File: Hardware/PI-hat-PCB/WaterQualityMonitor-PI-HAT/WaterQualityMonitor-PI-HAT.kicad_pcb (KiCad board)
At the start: 2 copper layers, 65 x 56 mm, 5 parts, among them J1 GPIO

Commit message: Started new pcb design
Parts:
- added C1: 10uF, SmacSYs:SOIC127P600X175-8N, F.Cu at (212.2, 87.9)
- added C10: 100n, Capacitor_SMD:C_1206_3216Metric_Pad1.33x1.80mm_HandSolder, F.Cu at (248.2, 114.3)
- added C11: 22u 10V, Capacitor_SMD:C_1206_3216Metric_Pad1.33x1.80mm_HandSolder, F.Cu at (245.3, 111.0)
- added C12: 22u 10V, Capacitor_SMD:C_1206_3216Metric_Pad1.33x1.80mm_HandSolder, F.Cu at (242.2, 120.9)
- added C13: 100n, Capacitor_SMD:C_1206_3216Metric_Pad1.33x1.80mm_HandSolder, F.Cu at (242.2, 117.4)
- added C14: 0.1uF, Capacitor_SMD:C_1206_3216Metric_Pad1.33x1.80mm_HandSolder, F.Cu at (310.8, 100.6)
- added C15: 0.1uF, Capacitor_SMD:C_1206_3216Metric_Pad1.33x1.80mm_HandSolder, F.Cu at (293.5, 122.5)
- added C16: 10u, Capacitor_SMD:C_1206_3216Metric_Pad1.33x1.80mm_HandSolder, F.Cu at (218.9, 117.8)
- added C17: 10u, Capacitor_SMD:C_1206_3216Metric_Pad1.33x1.80mm_HandSolder, F.Cu at (203.8, 126.8)
- added C18: 10u, Capacitor_SMD:C_1206_3216Metric_Pad1.33x1.80mm_HandSolder, F.Cu at (203.8, 130.1)
- added C19: 2.7n, Capacitor_SMD:C_1206_3216Metric_Pad1.33x1.80mm_HandSolder, F.Cu at (203.8, 133.5)
- added C2: 0.1uF, Capacitor_SMD:C_1206_3216Metric_Pad1.33x1.80mm_HandSolder, F.Cu at (226.4, 90.3)
- added C20: 100n, Capacitor_SMD:C_1206_3216Metric_Pad1.33x1.80mm_HandSolder, F.Cu at (223.3, 114.3)
- added C21: 22u 10V, Capacitor_SMD:C_1206_3216Metric_Pad1.33x1.80mm_HandSolder, F.Cu at (223.3, 111.0)
- added C22: 22u 10V, Capacitor_SMD:C_1206_3216Metric_Pad1.33x1.80mm_HandSolder, F.Cu at (212.9, 120.3)
- added C23: 100n, Capacitor_SMD:C_1206_3216Metric_Pad1.33x1.80mm_HandSolder, F.Cu at (209.8, 126.8)
- added C24: 100n, Capacitor_SMD:C_1206_3216Metric_Pad1.33x1.80mm_HandSolder, F.Cu at (217.3, 114.4)
- added C25: 100n, Capacitor_SMD:C_1206_3216Metric_Pad1.33x1.80mm_HandSolder, F.Cu at (221.8, 97.5)
- added C3: 47uF, Capacitor_SMD:C_1206_3216Metric_Pad1.33x1.80mm_HandSolder, F.Cu at (258.0, 65.8)
- added C4: 4.7uF, Capacitor_SMD:C_1206_3216Metric_Pad1.33x1.80mm_HandSolder, F.Cu at (249.2, 70.9)
- added C5: 10u, Capacitor_SMD:C_1206_3216Metric_Pad1.33x1.80mm_HandSolder, F.Cu at (269.1, 49.2)
- added C6: 10u, Capacitor_SMD:C_1206_3216Metric_Pad1.33x1.80mm_HandSolder, F.Cu at (236.2, 120.9)
- added C7: 10u, Capacitor_SMD:C_1206_3216Metric_Pad1.33x1.80mm_HandSolder, F.Cu at (251.3, 111.0)
- added C8: 10u, Capacitor_SMD:C_1206_3216Metric_Pad1.33x1.80mm_HandSolder, F.Cu at (236.2, 127.6)
- added C9: 2.7n, Capacitor_SMD:C_1206_3216Metric_Pad1.33x1.80mm_HandSolder, F.Cu at (236.2, 124.2)
- added D1: SESD0402X1UN-0020-090, SmacSYs:SESD0402X1UN0020090, F.Cu at (250.1, 74.7)
- added D2: OVLEW1CB9, SmacSYs:OVLEW1CB9, F.Cu at (212.9, 101.7)
- added D3: SMBJ26A, Snapeda:DIOM4336X265N, F.Cu at (250.9, 66.7)
- added F1: 0.5A, Fuse:Fuse_1206_3216Metric_Pad1.42x1.75mm_HandSolder, F.Cu at (245.2, 74.2)
- added F2: 4A, Fuse:Fuse_1206_3216Metric_Pad1.42x1.75mm_HandSolder, F.Cu at (232.4, 90.2)
- added F3: 3.2A, Fuse:Fuse_1206_3216Metric_Pad1.42x1.75mm_HandSolder, F.Cu at (255.2, 70.9)
- added F4: 10A, Fuse:Fuse_1206_3216Metric_Pad1.42x1.75mm_HandSolder, F.Cu at (226.4, 93.6)
- added FB1: 150uH, Inductor_SMD:L_1206_3216Metric_Pad1.22x1.90mm_HandSolder, F.Cu at (249.2, 59.8)
- added IC1: P82B96TD,118, SmacSYs:SOIC127P600X175-8N, F.Cu at (214.5, 94.5)
- added IC2: DMMT5401-7-F, SmacSYs:SOT95P285X140-6N, F.Cu at (235.8, 134.8)
- added J10: GPIO, Connector_PinSocket_2.54mm:PinSocket_2x20_P2.54mm_Vertical, F.Cu at (205.6, 46.4)
- added J2: Screw_Terminal_01x04, TerminalBlock:TerminalBlock_Altech_AK300-4_P5.00mm, F.Cu at (233.5, 51.1)
- added J3: Screw_Terminal_01x04, TerminalBlock:TerminalBlock_Altech_AK300-4_P5.00mm, F.Cu at (211.3, 51.1)
- added J4: Screw_Terminal_01x02, TerminalBlock:TerminalBlock_Altech_AK300-2_P5.00mm, F.Cu at (237.3, 65.0)
- added J5: Jack-DC 12V+, Connector_BarrelJack:BarrelJack_Wuerth_6941xx301002, F.Cu at (227.2, 60.0)
- added J6: SM04B-SRSS-TB(LF)(SN), Snapeda:JST_SM04B-SRSS-TB(LF)(SN), F.Cu at (238.1, 76.2)
- added JP1: ID_WP, Jumper:SolderJumper-2_P1.3mm_Open_RoundedPad1.0x1.5mm, F.Cu at (219.5, 79.8)
- added L1: 4.7uH, Inductor_SMD:L_1206_3216Metric_Pad1.22x1.90mm_HandSolder, F.Cu at (269.2, 45.8)
- added L2: 15u, Inductor_SMD:L_1206_3216Metric_Pad1.22x1.90mm_HandSolder, F.Cu at (236.2, 117.5)
- added L3: 15u, Inductor_SMD:L_1206_3216Metric_Pad1.22x1.90mm_HandSolder, F.Cu at (217.3, 111.0)
- added M1: Fan, Connector_PinHeader_2.54mm:PinHeader_1x02_P2.54mm_Vertical, F.Cu at (221.1, 90.9)
- added PE1: PeltierElement, TerminalBlock:TerminalBlock_Altech_AK300-2_P5.00mm, F.Cu at (225.0, 81.6)
- added PS1: TSR_2-2433, Converter_DCDC:Converter_DCDC_TRACO_TSR-1_THT, F.Cu at (205.1, 115.7)
- added Q1: IRL540SPBF, SmacSYs:IRL540SPBF, F.Cu at (259.3, 45.6)
- added Q2: IRL540SPBF, SmacSYs:IRL540SPBF, F.Cu at (214.8, 59.6)
- added Q3: DMG2305UX-7, Snapeda:SOT91P240X110-3N_DMG2305UX-7, F.Cu at (247.9, 124.8)
- added R1: 0.2, Resistor_SMD:R_1206_3216Metric_Pad1.30x1.75mm_HandSolder, F.Cu at (269.1, 52.5)
- added R10: 10k, Resistor_SMD:R_1206_3216Metric_Pad1.30x1.75mm_HandSolder, F.Cu at (236.1, 130.9)
- added R11: 10k, Resistor_SMD:R_1206_3216Metric_Pad1.30x1.75mm_HandSolder, F.Cu at (254.2, 114.3)
- added R12: 47K, Resistor_SMD:R_1206_3216Metric_Pad1.30x1.75mm_HandSolder, F.Cu at (257.3, 110.9)
- added R13: 178k, Resistor_SMD:R_1206_3216Metric_Pad1.30x1.75mm_HandSolder, F.Cu at (203.8, 136.8)
- added R14: 10k, Resistor_SMD:R_1206_3216Metric_Pad1.30x1.75mm_HandSolder, F.Cu at (209.8, 130.1)
- added R15: 24k, Resistor_SMD:R_1206_3216Metric_Pad1.30x1.75mm_HandSolder, F.Cu at (215.8, 124.4)
- added R16: 10k, Resistor_SMD:R_1206_3216Metric_Pad1.30x1.75mm_HandSolder, F.Cu at (224.9, 117.6)
- added R17: 1k87, Resistor_SMD:R_1206_3216Metric_Pad1.30x1.75mm_HandSolder, F.Cu at (218.9, 121.1)
- added R18: 3.9k, Resistor_SMD:R_1206_3216Metric_Pad1.30x1.75mm_HandSolder, F.Cu at (245.2, 77.5)
- added R19: 3.9k, Resistor_SMD:R_1206_3216Metric_Pad1.30x1.75mm_HandSolder, F.Cu at (236.9, 83.3)
- added R2: 5.1, Resistor_SMD:R_1206_3216Metric_Pad1.30x1.75mm_HandSolder, F.Cu at (221.1, 100.8)
- added R3: 1.20KOHM-0603-1_10W-1%, Resistor_SMD:R_1206_3216Metric_Pad1.30x1.75mm_HandSolder, F.Cu at (236.9, 86.6)
- added R4: 10K, Resistor_SMD:R_1206_3216Metric_Pad1.30x1.75mm_HandSolder, F.Cu at (275.2, 45.7)
- added R5: 10K, Resistor_SMD:R_1206_3216Metric_Pad1.30x1.75mm_HandSolder, F.Cu at (275.2, 49.0)
- added R6: 178k, Resistor_SMD:R_1206_3216Metric_Pad1.30x1.75mm_HandSolder, F.Cu at (242.1, 124.2)
- added R7: 24k, Resistor_SMD:R_1206_3216Metric_Pad1.30x1.75mm_HandSolder, F.Cu at (248.2, 117.6)
- added R8: 10k, Resistor_SMD:R_1206_3216Metric_Pad1.30x1.75mm_HandSolder, F.Cu at (242.1, 127.5)
- added R9: 1k87, Resistor_SMD:R_1206_3216Metric_Pad1.30x1.75mm_HandSolder, F.Cu at (248.1, 120.9)
- added U1: DRV8870DDA, Package_SO:Texas_HTSOP-8-1EP_3.9x4.9mm_P1.27mm_EP2.95x4.9mm_Mask2.4x3.1mm_ThermalVias, F.Cu at (205.5, 100.2)
- added U2: TPS61169DCKR, Snapeda:SOT65P210X110-5N, F.Cu at (219.3, 86.5)
- added U3: TMC2208_SILENTSTEPSTICK, Footprints:TMC2208_SILENTSTEPSTICK, F.Cu at (298.9, 76.9)
- added U4: TMC2208_SILENTSTEPSTICK, Footprints:TMC2208_SILENTSTEPSTICK, F.Cu at (298.9, 55.0)
- added U5: RT7272AGSP, Snapeda:SOIC127P599X175-9N, F.Cu at (238.0, 112.5)
- added U6: TMC2208_SILENTSTEPSTICK, Footprints:TMC2208_SILENTSTEPSTICK, F.Cu at (298.9, 109.8)
- added U7: DRV8838, Package_SON:WSON-8-1EP_2x2mm_P0.5mm_EP0.9x1.6mm, F.Cu at (292.6, 125.9)
- added U8: RT7272AGSP, Snapeda:SOIC127P599X175-9N, F.Cu at (205.7, 121.9)
- added U9: CAT24C256, Footprints:SOIC127P600X175-8N, F.Cu at (213.1, 81.3)
- J1: value GPIO -> Screw_Terminal_01x04; footprint Connector_PinSocket_2.54mm:PinSocket_2x20_P2.54mm_Vertical -> TerminalBlock:TerminalBlock_Altech_AK300-4_P5.00mm
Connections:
- J1 pad 1: +3V3 -> /FluidMotors/OA1MAIN
- J1 pad 2: +5V -> /FluidMotors/OA2MAIN
- J1 pad 3: /GPIO[2]/SDA1 -> /FluidMotors/OB1MAIN
- J1 pad 4: +5V -> /FluidMotors/OB2MAIN

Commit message: standard pi hat layout finsished
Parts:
- moved J1 254.1 mm to (338.9, 155.5)
- moved C18 90.8 mm to (192.0, 220.2)
- moved J5 90.8 mm to (215.4, 150.1)
- moved L1 90.8 mm to (257.4, 135.9)
- moved Q2 90.8 mm to (203.0, 149.7)
- moved R1 90.8 mm to (257.3, 142.6)
- moved C11 90.8 mm to (233.5, 201.0)
- moved C12 90.8 mm to (230.3, 210.9)
- moved C15 90.8 mm to (281.7, 212.5)
- moved C16 90.8 mm to (207.1, 207.8)
- moved C17 90.8 mm to (192.0, 216.9)
- moved C2 90.8 mm to (214.6, 180.3)
- moved C21 90.8 mm to (211.5, 201.0)
- moved C23 90.8 mm to (198.0, 216.9)
- moved C3 90.8 mm to (246.2, 155.8)
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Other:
- board text removed: "Extend PCB edge 0.5mm if using SMT header"

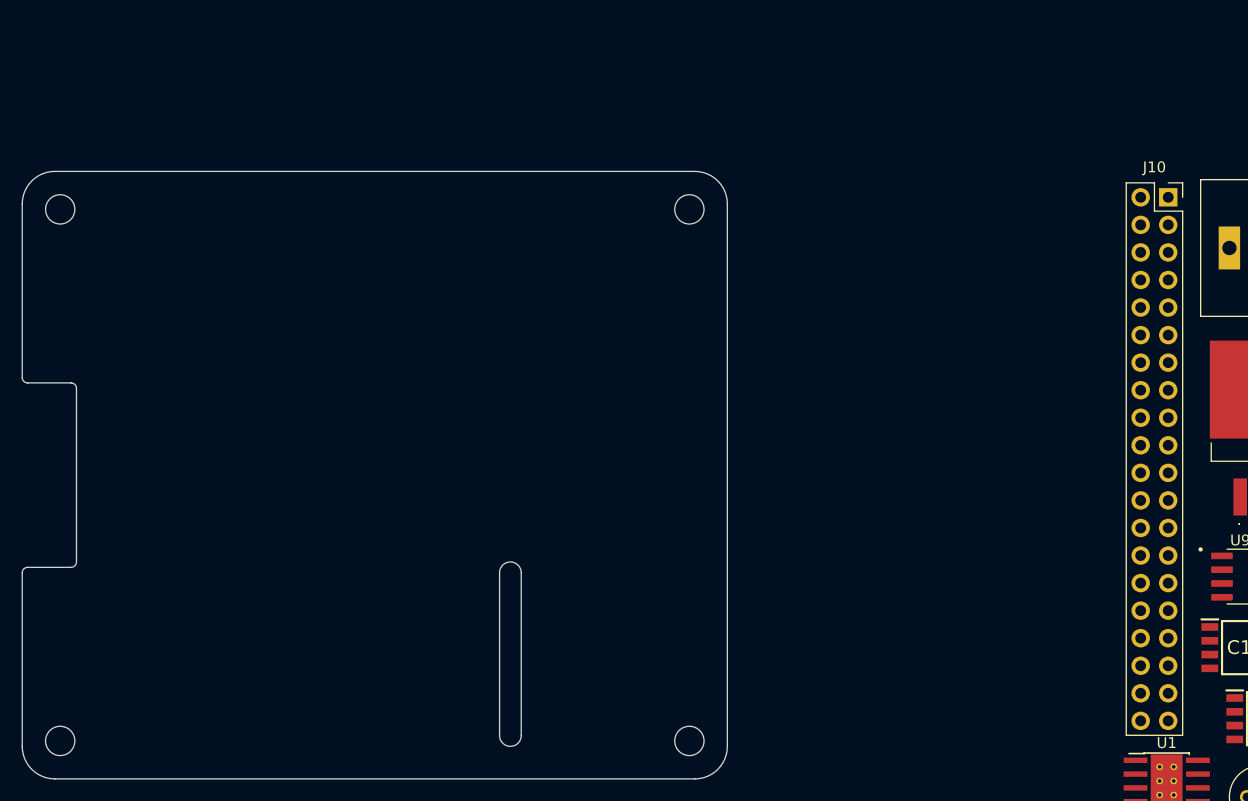
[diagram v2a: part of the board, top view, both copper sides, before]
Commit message: GPIO header moved, hopefully centered
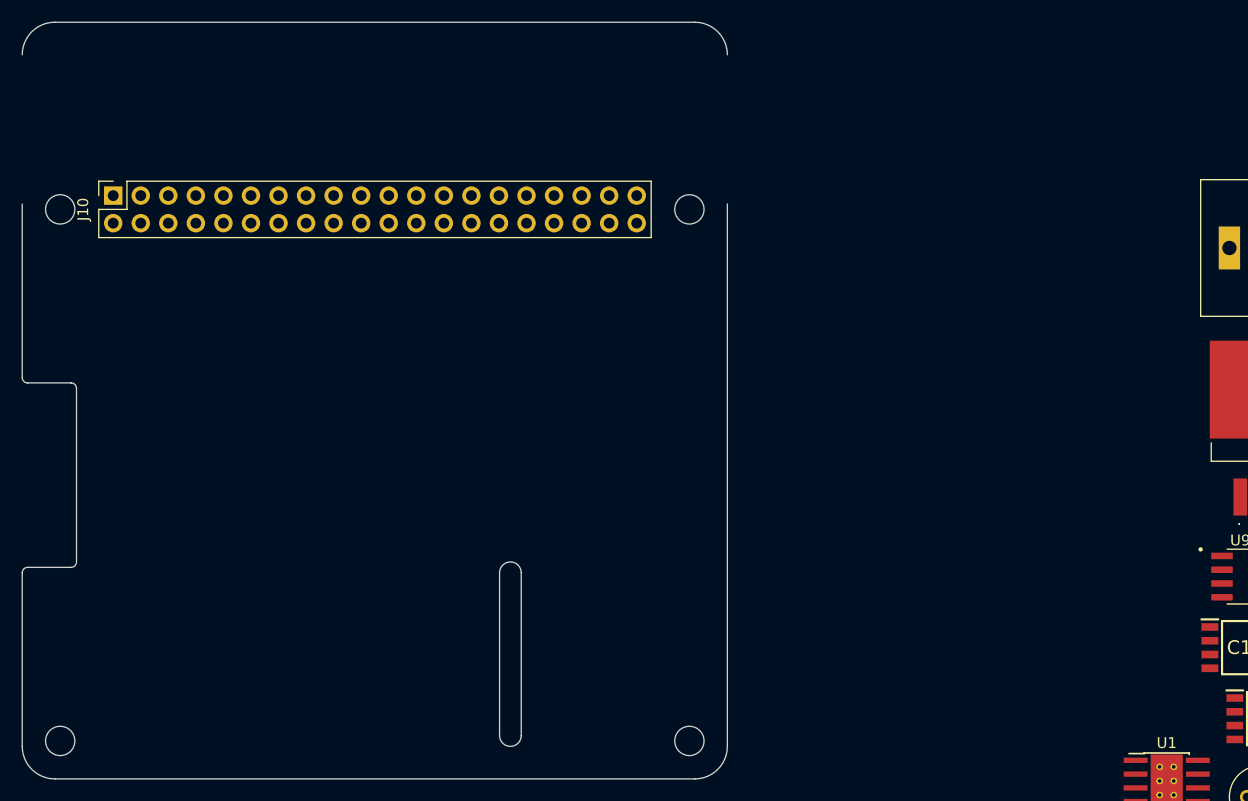
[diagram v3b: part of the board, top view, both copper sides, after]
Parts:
- moved J10 97.3 mm to (96.6, 136.3), turned to 90 degrees
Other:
- board size 65 x 56 mm -> 65 x 69.8 mm

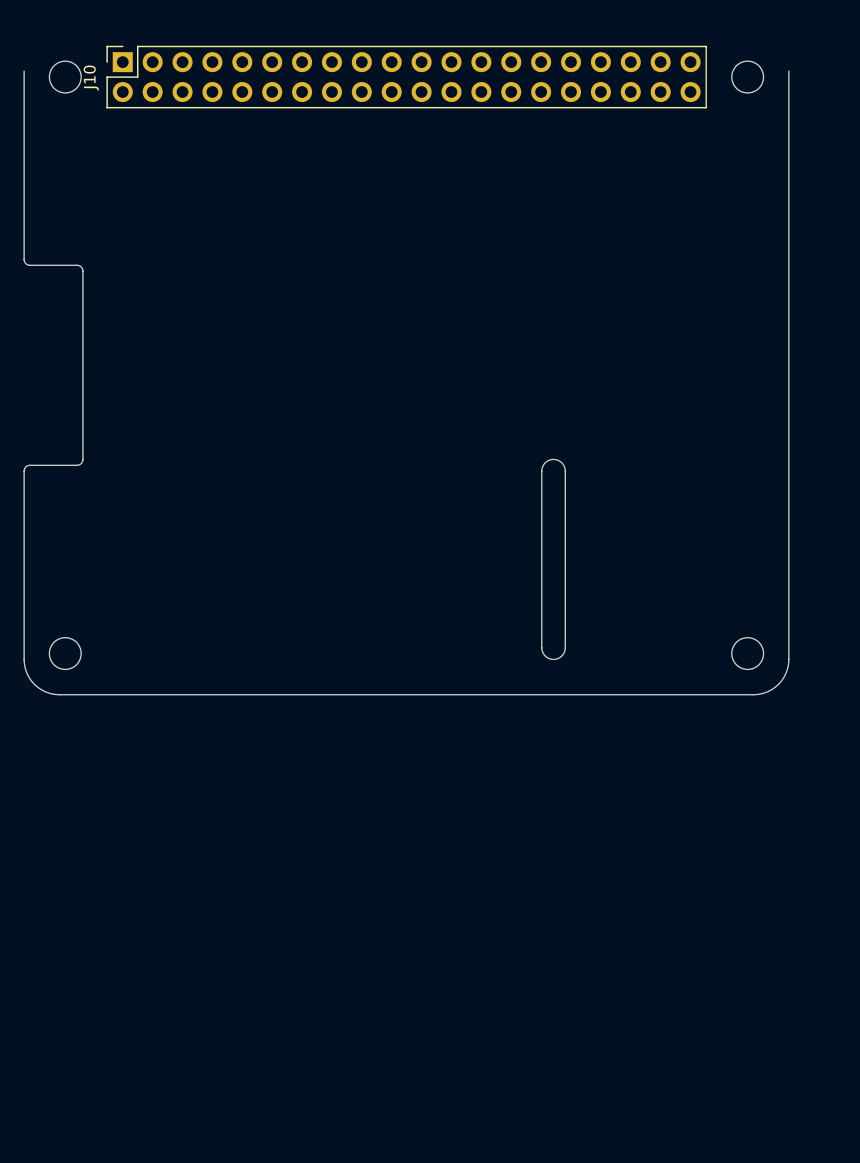
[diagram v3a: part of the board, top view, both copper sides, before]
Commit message: Enlarged hat even further
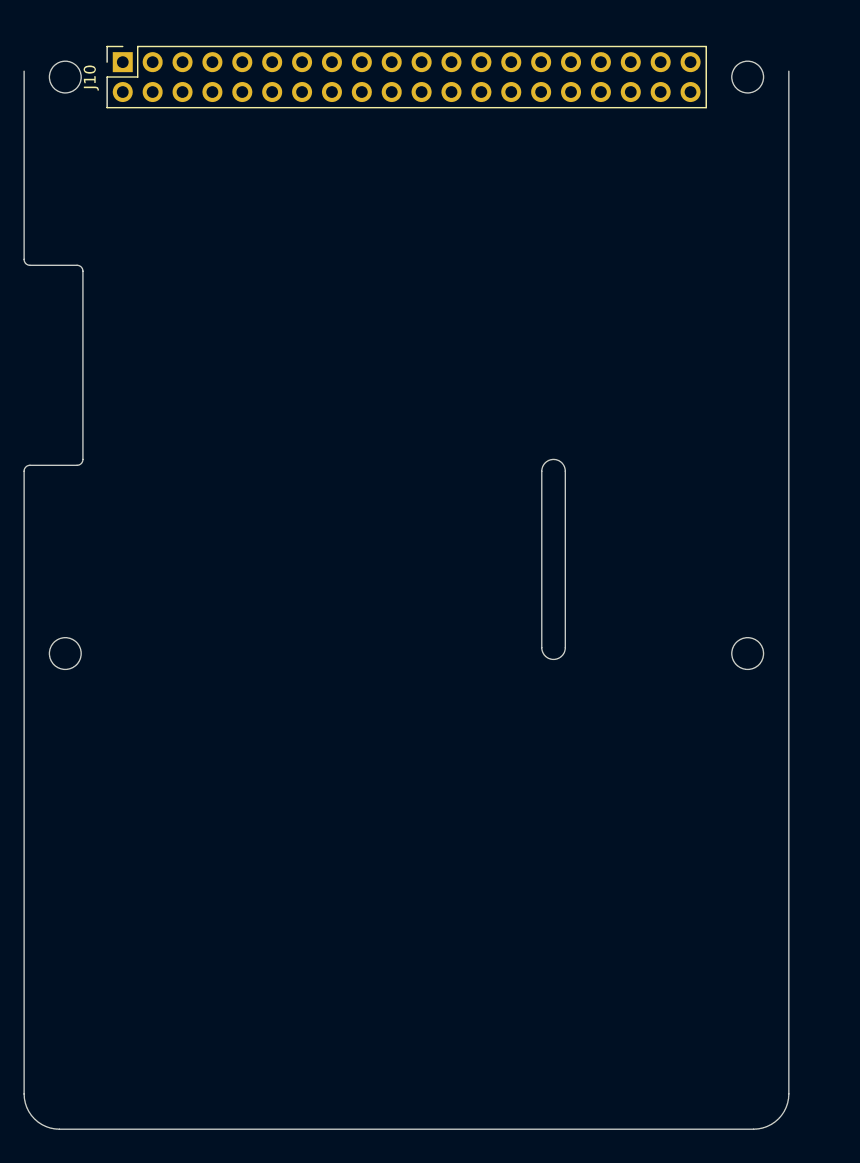
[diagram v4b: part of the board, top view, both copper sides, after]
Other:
- board size 65 x 69.8 mm -> 65 x 106.7 mm
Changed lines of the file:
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@@
   (gr_arc (start 88.69 153.57) (mid 88.336447 153.423553) (end 88.19 153.07) (layer "Edge.Cuts") (width 0.1))
   (gr_arc (start 150.19 120.32) (mid 152.31132 121.19868) (end 153.19 123.32) (layer "Edge.Cuts") (width 0.1))
-  (gr_line (start 153.19 187.07) (end 153.19 137.07) (layer "Edge.Cuts") (width 0.1))
+  (gr_line (start 153.19 224) (end 153.19 137.07) (layer "Edge.Cuts") (width 0.1))
   (gr_line (start 88.19 137.07) (end 88.19 153.07) (layer "Edge.Cuts") (width 0.1))
   (gr_line (start 134.19 171.07) (end 134.19 186.07) (layer "Edge.Cuts") (width 0.1))
   (gr_line (start 132.19 186.07) (end 132.19 171.07) (layer "Edge.Cuts") (width 0.1))
-  (gr_arc (start 91.19 190.07) (mid 89.06868 189.19132) (end 88.19 187.07) (layer "Edge.Cuts") (width 0.1))
-  (gr_line (start 91.19 190.07) (end 150.19 190.07) (layer "Edge.Cuts") (width 0.1))
+  (gr_arc (start 91.19 227) (mid 89.06868 226.12132) (end 88.19 224) (layer "Edge.Cuts") (width 0.1))
+  (gr_line (start 91.19 227) (end 150.19 227) (layer "Edge.Cuts") (width 0.1))
   (gr_line (start 92.69 170.57) (end 88.69 170.57) (layer "Edge.Cuts") (width 0.1))
   (gr_arc (start 132.19 171.07) (mid 133.19 170.07) (end 134.19 171.07) (layer "Edge.Cuts") (width 0.1))
   (gr_arc (start 88.19 171.07) (mid 88.336138 170.716755) (end 88.689127 170.570001) (layer "Edge.Cuts") (width 0.1))
-  (gr_arc (start 153.19 187.07) (mid 152.31132 189.19132) (end 150.19 190.07) (layer "Edge.Cuts") (width 0.1))
+  (gr_arc (start 153.19 224) (mid 152.31132 226.12132) (end 150.19 227) (layer "Edge.Cuts") (width 0.1))
   (gr_line (start 93.19 154.07) (end 93.19 170.07) (layer "Edge.Cuts") (width 0.1))
   (gr_arc (start 88.19 123.32) (mid 89.06868 121.19868) (end 91.19 120.32) (layer "Edge.Cuts") (width 0.1))
   (gr_arc (start 134.19 186.07) (mid 133.19 187.07) (end 132.19 186.07) (layer "Edge.Cuts") (width 0.1))
-  (gr_line (start 88.19 171.07) (end 88.19 187.07) (layer "Edge.Cuts") (width 0.1))
+  (gr_line (start 88.19 171.07) (end 88.19 224) (layer "Edge.Cuts") (width 0.1))
   (gr_line (start 88.69 153.57) (end 92.69 153.57) (layer "Edge.Cuts") (width 0.1))
   (gr_arc (start 93.19 170.07) (mid 93.043553 170.423553) (end 92.69 170.57) (layer "Edge.Cuts") (width 0.1))
